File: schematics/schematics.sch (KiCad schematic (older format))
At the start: 3 parts

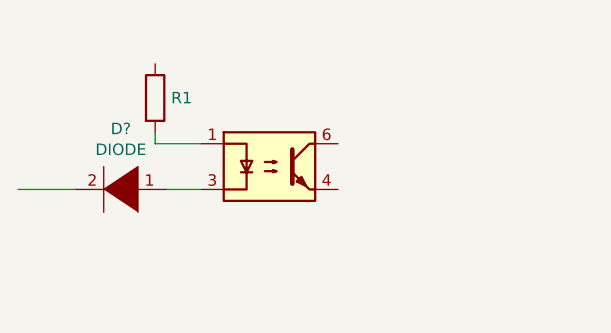
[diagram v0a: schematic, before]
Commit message: Edit the circuit for the pump
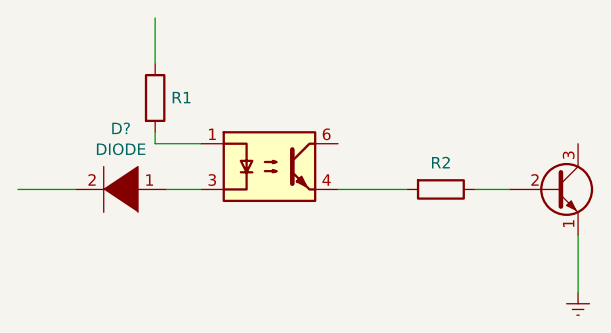
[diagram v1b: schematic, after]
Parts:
- added Q?: 2N2219, Package_TO_SOT_THT:TO-39-3, symbol Transistor_BJT:2N2219
- added R2: R, symbol Device:R
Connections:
- net labels added: GNDREF
- wire segments 4 -> 8
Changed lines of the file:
@@
 Wire Wire Line
 	4350 4700 4100 4700
+Wire Wire Line
+	4700 4150 4700 3950
+Wire Wire Line
+	5500 4700 5800 4700
+$Comp
+L Device:R R2
+U 1 1 5C8C515D
+P 5950 4700
+F 0 "R2" V 5835 4700 50  0000 C CNN
+F 1 "R" V 5834 4700 50  0001 C CNN
+F 2 "" V 5880 4700 50  0001 C CNN
+F 3 "~" H 5950 4700 50  0001 C CNN
+	1    5950 4700
+	0    1    1    0
+$EndComp
+Wire Wire Line
+	6100 4700 6250 4700
+$Comp
+L Transistor_BJT:2N2219 Q?
+U 1 1 5C8C7983
+P 6450 4700
+F 0 "Q?" H 6640 4746 50  0001 L CNN
+F 1 "2N2219" H 6640 4700 50  0001 L CNN
+F 2 "Package_TO_SOT_THT:TO-39-3" H 6650 4625 50  0001 L CIN
+F 3 "http://www.onsemi.com/pub_link/Collateral/2N2219-D.PDF" H 6450 4700 50  0001 L CNN
+	1    6450 4700
+	1    0    0    -1
+$EndComp
+Wire Wire Line
+	6550 4900 6550 5150
+$Comp
+L power:GNDREF #PWR?
+U 1 1 5C8C8969
+P 6550 5150
+F 0 "#PWR?" H 6550 4900 50  0001 C CNN
+F 1 "GNDREF" H 6555 4977 50  0001 C CNN
+F 2 "" H 6550 5150 50  0001 C CNN
+F 3 "" H 6550 5150 50  0001 C CNN
+	1    6550 5150
+	1    0    0    -1
+$EndComp
 $EndSCHEMATC

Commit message: Edit the base of the circuit
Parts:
- D?: value DIODE -> DS1
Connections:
- net labels added: VCC
- wire segments 8 -> 13
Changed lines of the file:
@@
 EESchema Schematic File Version 4
+LIBS:schematics-cache
 EELAYER 29 0
 EELAYER END
@@
 U 1 1 5C8C1EFD
 P 4550 4700
-F 0 "D?" H 4550 4435 50  0000 C CNN
-F 1 "DIODE" H 4550 4526 50  0000 C CNN
+F 0 "D?" H 4550 4435 50  0001 C CNN
+F 1 "DS1" H 4550 4526 50  0000 C CNN
 F 2 "" H 4550 4700 50  0001 C CNN
 F 3 "~" H 4550 4700 50  0001 C CNN
@@
 Wire Wire Line
 	4350 4700 4100 4700
-Wire Wire Line
-	4700 4150 4700 3950
 Wire Wire Line
 	5500 4700 5800 4700
@@
 F 3 "~" H 5950 4700 50  0001 C CNN
 	1    5950 4700
-	0    1    1    0
+	0    1    -1   0
 $EndComp
 Wire Wire Line
@@
 	1    0    0    -1
 $EndComp
+$Comp
+L power:VCC #PWR?
+U 1 1 5C8BCB84
+P 4700 3800
+F 0 "#PWR?" H 4700 3650 50  0001 C CNN
+F 1 "VCC" H 4717 3973 50  0000 C CNN
+F 2 "" H 4700 3800 50  0001 C CNN
+F 3 "" H 4700 3800 50  0001 C CNN
+	1    4700 3800
+	1    0    0    -1
+$EndComp
+Wire Wire Line
+	4700 3800 4250 3800
+Connection ~ 4700 3800
+$Comp
+L power:VCC #PWR?
+U 1 1 5C8BE04C
+P 4250 3800
+F 0 "#PWR?" H 4250 3650 50  0001 C CNN
+F 1 "VCC" V 4268 3927 50  0001 L CNN
+F 2 "" H 4250 3800 50  0001 C CNN
+F 3 "" H 4250 3800 50  0001 C CNN
+	1    4250 3800
+	0    -1   -1   0
+$EndComp
+Wire Wire Line
+	4700 3800 4700 4150
+Wire Wire Line
+	5500 4500 5600 4500
+Wire Wire Line
+	5600 4500 5600 4100
+Wire Wire Line
+	5600 4100 5300 4100
+Wire Wire Line
+	5300 4100 5300 3800
+$Comp
+L power:VCC #PWR?
+U 1 1 5C8C0019
+P 5300 3800
+F 0 "#PWR?" H 5300 3650 50  0001 C CNN
+F 1 "VCC" H 5317 3973 50  0000 C CNN
+F 2 "" H 5300 3800 50  0001 C CNN
+F 3 "" H 5300 3800 50  0001 C CNN
+	1    5300 3800
+	1    0    0    -1
+$EndComp

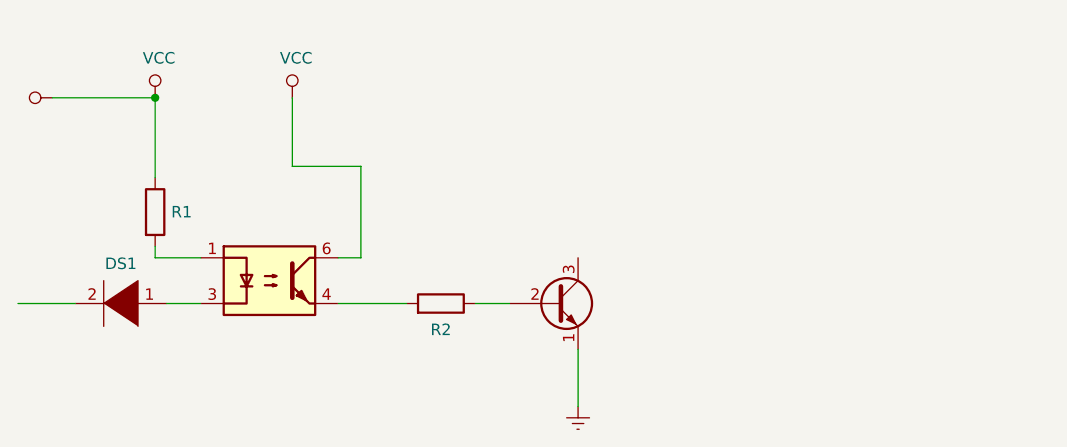
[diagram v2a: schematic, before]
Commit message: Edit the pump circuit
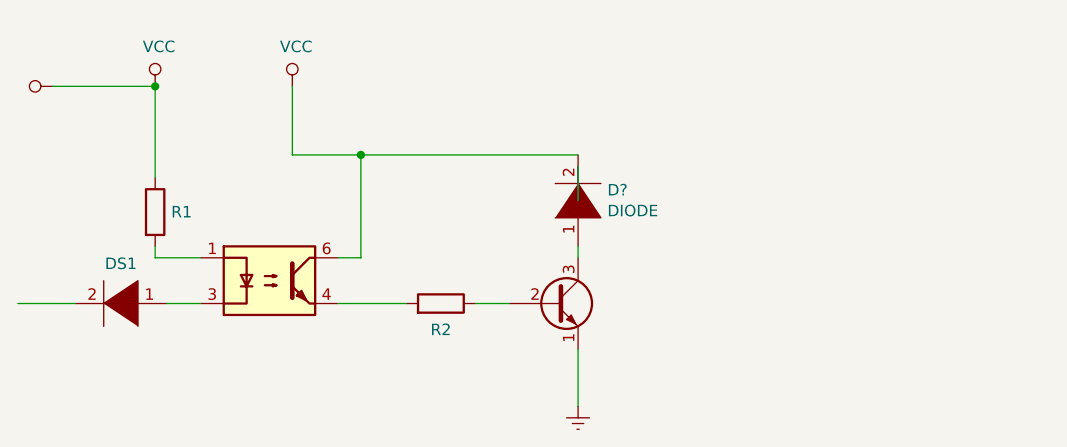
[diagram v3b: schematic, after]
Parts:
- added D?: DIODE, symbol pspice:DIODE
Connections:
- wire segments 13 -> 16
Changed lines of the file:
@@
 L power:VCC #PWR?
 U 1 1 5C8BCB84
-P 4700 3800
-F 0 "#PWR?" H 4700 3650 50  0001 C CNN
-F 1 "VCC" H 4717 3973 50  0000 C CNN
-F 2 "" H 4700 3800 50  0001 C CNN
-F 3 "" H 4700 3800 50  0001 C CNN
-	1    4700 3800
+P 4700 3750
+F 0 "#PWR?" H 4700 3600 50  0001 C CNN
+F 1 "VCC" H 4717 3923 50  0000 C CNN
+F 2 "" H 4700 3750 50  0001 C CNN
+F 3 "" H 4700 3750 50  0001 C CNN
+	1    4700 3750
 	1    0    0    -1
 $EndComp
 Wire Wire Line
-	4700 3800 4250 3800
-Connection ~ 4700 3800
+	4700 3750 4250 3750
+Connection ~ 4700 3750
 $Comp
 L power:VCC #PWR?
 U 1 1 5C8BE04C
-P 4250 3800
-F 0 "#PWR?" H 4250 3650 50  0001 C CNN
-F 1 "VCC" V 4268 3927 50  0001 L CNN
-F 2 "" H 4250 3800 50  0001 C CNN
-F 3 "" H 4250 3800 50  0001 C CNN
-	1    4250 3800
+P 4250 3750
+F 0 "#PWR?" H 4250 3600 50  0001 C CNN
+F 1 "VCC" V 4268 3877 50  0001 L CNN
+F 2 "" H 4250 3750 50  0001 C CNN
+F 3 "" H 4250 3750 50  0001 C CNN
+	1    4250 3750
 	0    -1   -1   0
 $EndComp
 Wire Wire Line
-	4700 3800 4700 4150
-Wire Wire Line
 	5500 4500 5600 4500
 Wire Wire Line
-	5600 4500 5600 4100
-Wire Wire Line
-	5600 4100 5300 4100
-Wire Wire Line
-	5300 4100 5300 3800
+	5600 4050 5300 4050
 $Comp
 L power:VCC #PWR?
 U 1 1 5C8C0019
-P 5300 3800
-F 0 "#PWR?" H 5300 3650 50  0001 C CNN
-F 1 "VCC" H 5317 3973 50  0000 C CNN
-F 2 "" H 5300 3800 50  0001 C CNN
-F 3 "" H 5300 3800 50  0001 C CNN
-	1    5300 3800
+P 5300 3750
+F 0 "#PWR?" H 5300 3600 50  0001 C CNN
+F 1 "VCC" H 5317 3923 50  0000 C CNN
+F 2 "" H 5300 3750 50  0001 C CNN
+F 3 "" H 5300 3750 50  0001 C CNN
+	1    5300 3750
 	1    0    0    -1
 $EndComp
+Wire Wire Line
+	5600 4050 6550 4050
+Connection ~ 5600 4050
+Wire Wire Line
+	6550 4500 6550 4450
+$Comp
+L pspice:DIODE D?
+U 1 1 5C8C3A6E
+P 6550 4250
+F 0 "D?" V 6596 4122 50  0000 R CNN
+F 1 "DIODE" V 6505 4122 50  0000 R CNN
+F 2 "" H 6550 4250 50  0001 C CNN
+F 3 "~" H 6550 4250 50  0001 C CNN
+	1    6550 4250
+	0    -1   -1   0
+$EndComp
+Wire Wire Line
+	5300 3750 5300 4050
+Wire Wire Line
+	4700 3750 4700 4150
+Wire Wire Line
+	5600 4050 5600 4500
+Wire Wire Line
+	6550 4100 6550 4250
 $EndSCHEMATC

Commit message: Final wersion of the pump circuit
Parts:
- added JP?: Jumper, symbol Device:Jumper
- added K?: DIPxx-1Cxx-51x, Relay_THT:Relay_StandexMeder_DIP_LowProfile, symbol Relay:DIPxx-1Cxx-51x
- gave numbers to parts that had none: 1
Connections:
- wire segments 16 -> 21
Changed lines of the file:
@@
-	1    0    0    -1
-$EndComp
-$Comp
-L power:VCC #PWR?
-U 1 1 5C8BCB84
-P 4700 3750
-F 0 "#PWR?" H 4700 3600 50  0001 C CNN
-F 1 "VCC" H 4717 3923 50  0000 C CNN
-F 2 "" H 4700 3750 50  0001 C CNN
-F 3 "" H 4700 3750 50  0001 C CNN
-	1    4700 3750
 	1    0    0    -1
 $EndComp
 Wire Wire Line
-	4700 3750 4250 3750
-Connection ~ 4700 3750
+	4700 3550 4250 3550
 $Comp
 L power:VCC #PWR?
 U 1 1 5C8BE04C
-P 4250 3750
-F 0 "#PWR?" H 4250 3600 50  0001 C CNN
-F 1 "VCC" V 4268 3877 50  0001 L CNN
-F 2 "" H 4250 3750 50  0001 C CNN
-F 3 "" H 4250 3750 50  0001 C CNN
-	1    4250 3750
+P 4250 3550
+F 0 "#PWR?" H 4250 3400 50  0001 C CNN
+F 1 "VCC" V 4268 3677 50  0001 L CNN
+F 2 "" H 4250 3550 50  0001 C CNN
+F 3 "" H 4250 3550 50  0001 C CNN
+	1    4250 3550
 	0    -1   -1   0
 $EndComp
@@
 	5500 4500 5600 4500
 Wire Wire Line
-	5600 4050 5300 4050
-$Comp
-L power:VCC #PWR?
-U 1 1 5C8C0019
-P 5300 3750
-F 0 "#PWR?" H 5300 3600 50  0001 C CNN
-F 1 "VCC" H 5317 3923 50  0000 C CNN
-F 2 "" H 5300 3750 50  0001 C CNN
-F 3 "" H 5300 3750 50  0001 C CNN
-	1    5300 3750
-	1    0    0    -1
-$EndComp
-Wire Wire Line
-	5600 4050 6550 4050
-Connection ~ 5600 4050
-Wire Wire Line
 	6550 4500 6550 4450
 $Comp
-L pspice:DIODE D?
+L pspice:DIODE D1
 U 1 1 5C8C3A6E
 P 6550 4250
-F 0 "D?" V 6596 4122 50  0000 R CNN
-F 1 "DIODE" V 6505 4122 50  0000 R CNN
+F 0 "D1" V 6550 4122 50  0000 R CNN
+F 1 "DIODE" V 6505 4122 50  0001 R CNN
 F 2 "" H 6550 4250 50  0001 C CNN
 F 3 "~" H 6550 4250 50  0001 C CNN
@@
 $EndComp
 Wire Wire Line
-	5300 3750 5300 4050
+	6550 4100 6550 4250
+$Comp
+L Device:Jumper JP?
+U 1 1 5C8CFC95
+P 5000 3550
+F 0 "JP?" H 5000 3814 50  0001 C CNN
+F 1 "Jumper" H 5000 3723 50  0001 C CNN
+F 2 "" H 5000 3550 50  0001 C CNN
+F 3 "~" H 5000 3550 50  0001 C CNN
+	1    5000 3550
+	1    0    0    -1
+$EndComp
+$Comp
+L Relay:DIPxx-1Cxx-51x K?
+U 1 1 5C8D3DB8
+P 7450 4200
+F 0 "K?" H 7880 4246 50  0000 L CNN
+F 1 "DIPxx-1Cxx-51x" H 7880 4155 50  0000 L CNN
+F 2 "Relay_THT:Relay_StandexMeder_DIP_LowProfile" H 7900 4150 50  0001 L CNN
+F 3 "https://standexelectronics.com/wp-content/uploads/datasheet_reed_relay_DIP.pdf" H 7450 4200 50  0001 C CNN
+	1    7450 4200
+	1    0    0    -1
+$EndComp
 Wire Wire Line
-	4700 3750 4700 4150
+	5300 3900 5600 3900
 Wire Wire Line
-	5600 4050 5600 4500
+	5300 3550 5300 3900
 Wire Wire Line
-	6550 4100 6550 4250
+	6550 4050 6550 3900
+Wire Wire Line
+	4700 3550 4700 4150
+Connection ~ 4700 3550
+Wire Wire Line
+	5600 3900 5600 4500
+Connection ~ 5600 3900
+Wire Wire Line
+	5600 3900 6550 3900
+Wire Wire Line
+	7250 3900 6550 3900
+Connection ~ 6550 3900
+Wire Wire Line
+	7250 4500 6650 4500
+Wire Wire Line
+	6650 4500 6650 4450
+Wire Wire Line
+	6650 4450 6550 4450
+Connection ~ 6550 4450
 $EndSCHEMATC
